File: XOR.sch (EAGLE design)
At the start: 60 parts, among them IC1 40106D, IC2 4030D, IC3 4520D, IC7 TL074D

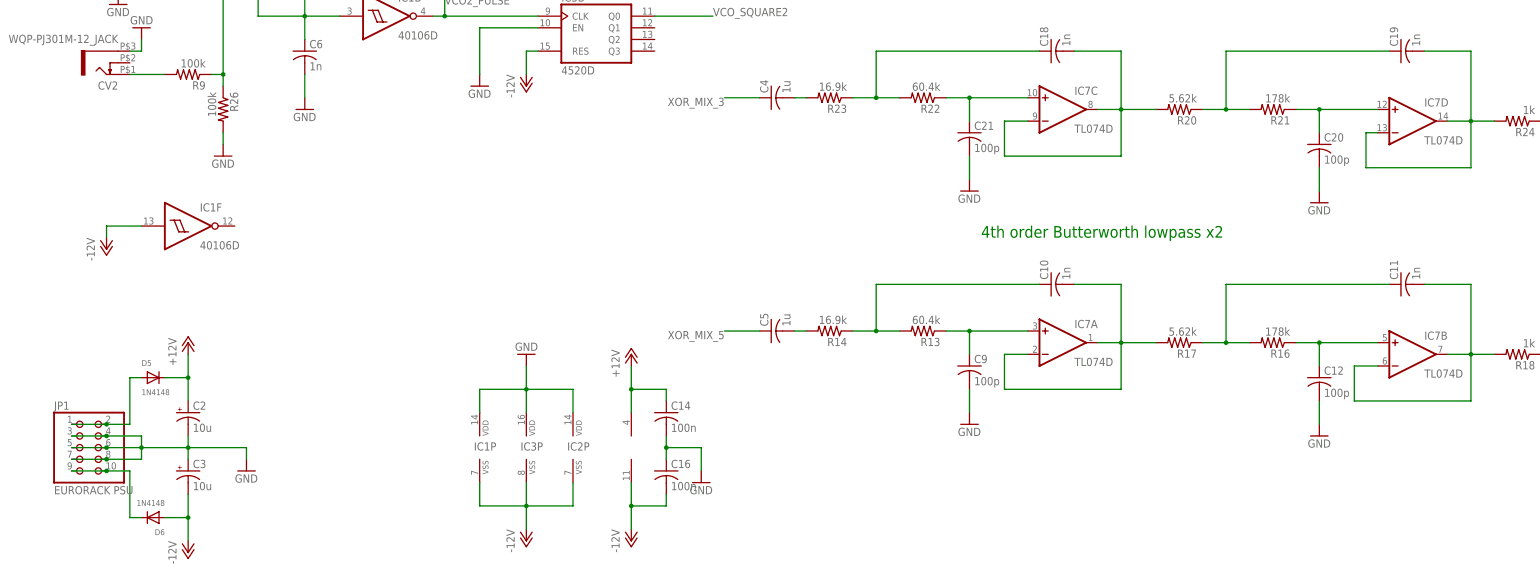
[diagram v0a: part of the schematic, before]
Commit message: added decoupling caps at logic ICs.
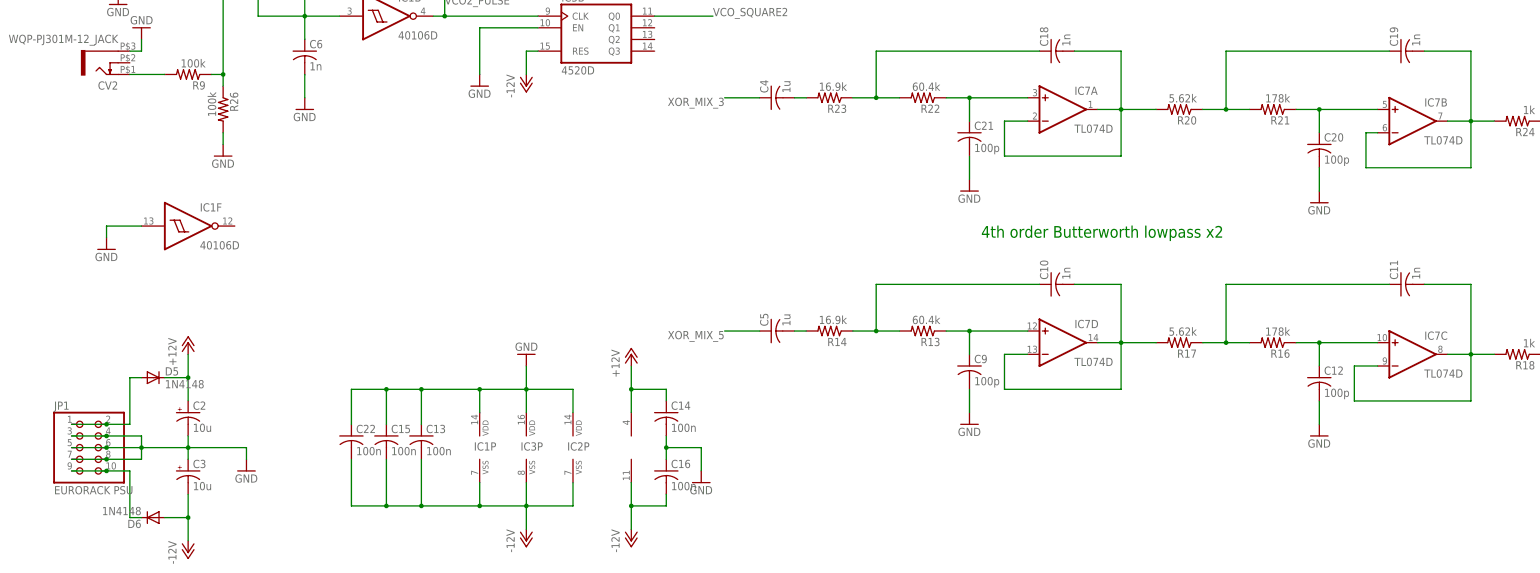
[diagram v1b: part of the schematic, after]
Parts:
- added C13, C15, C22: 100n, rcl:C-USC0603K
- D5, D6: device adafruit:DIODESOD-323F -> diode:DIODE-DO214AA
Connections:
- net -12V: now also C13.2, C15.2, C22.2; no longer IC1F.I
- net GND: now also C13.1, C15.1, C22.1, IC1F.I
- net N$16: now also IC7C.+IN; no longer IC7B.+IN
- net N$18: now also IC7D.-IN, IC7D.OUT; no longer IC7A.-IN, IC7A.OUT
- net N$22: now also IC7D.+IN; no longer IC7A.+IN
- net N$29: now also IC7A.-IN, IC7A.OUT; no longer IC7C.-IN, IC7C.OUT
- net N$30: now also IC7A.+IN; no longer IC7C.+IN
- net N$32: now also IC7C.-IN, IC7C.OUT; no longer IC7B.-IN, IC7B.OUT
- net N$35: now also IC7B.+IN; no longer IC7D.+IN
- net N$36: now also IC7B.-IN, IC7B.OUT; no longer IC7D.-IN, IC7D.OUT
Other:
- moved on the sheet: IC7A, IC7B, IC7C, IC7D
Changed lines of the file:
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@@
 <part name="GND13" library="supply1" deviceset="GND" device=""/>
 <part name="GND14" library="supply1" deviceset="GND" device=""/>
-<part name="D5" library="adafruit" deviceset="DIODE" device="SOD-323F" value="1N4148"/>
-<part name="D6" library="adafruit" deviceset="DIODE" device="SOD-323F" value="1N4148"/>
+<part name="D5" library="diode" deviceset="DIODE-" device="DO214AA" value="1N4148"/>
+<part name="D6" library="diode" deviceset="DIODE-" device="DO214AA" value="1N4148"/>
 <part name="D7" library="adafruit" deviceset="DIODE" device="SOD-323F" value="1N4148"/>
 <part name="D8" library="adafruit" deviceset="DIODE" device="SOD-323F" value="1N4148"/>
@@
 <part name="C4" library="rcl" deviceset="C-US" device="C0603K" value="1u"/>
 <part name="C5" library="rcl" deviceset="C-US" device="C0603K" value="1u"/>
-<part name="P-2" library="supply1" deviceset="-12V" device=""/>
 <part name="P-3" library="supply1" deviceset="-12V" device=""/>
 <part name="P-4" library="supply1" deviceset="-12V" device=""/>
@@
 <part name="P+1" library="supply1" deviceset="+12V" device=""/>
 <part name="P+2" library="supply1" deviceset="+12V" device=""/>
+<part name="GND23" library="supply1" deviceset="GND" device=""/>
+<part name="C13" library="rcl" deviceset="C-US" device="C0603K" value="100n"/>
+<part name="C15" library="rcl" deviceset="C-US" device="C0603K" value="100n"/>
+<part name="C22" library="rcl" deviceset="C-US" device="C0603K" value="100n"/>
 </parts>
 <sheets>
@@
 <instance part="C7" gate="G$1" x="208.28" y="193.04"/>
 <instance part="C17" gate="G$1" x="299.72" y="193.04"/>
-<instance part="IC7" gate="A" x="238.76" y="63.5"/>
-<instance part="IC7" gate="B" x="314.96" y="60.96"/>
-<instance part="IC7" gate="C" x="238.76" y="114.3"/>
-<instance part="IC7" gate="D" x="314.96" y="111.76"/>
+<instance part="IC7" gate="D" x="238.76" y="63.5"/>
+<instance part="IC7" gate="C" x="314.96" y="60.96"/>
+<instance part="IC7" gate="A" x="238.76" y="114.3"/>
+<instance part="IC7" gate="B" x="314.96" y="111.76"/>
 <instance part="IC7" gate="P" x="144.78" y="40.64"/>
 <instance part="C18" gate="G$1" x="236.22" y="127" rot="R90"/>
@@
 <instance part="C4" gate="G$1" x="175.26" y="116.84" rot="R90"/>
 <instance part="C5" gate="G$1" x="175.26" y="66.04" rot="R90"/>
-<instance part="P-2" gate="1" x="30.48" y="83.82"/>
 <instance part="P-3" gate="1" x="121.92" y="190.5"/>
 <instance part="P-4" gate="1" x="121.92" y="119.38"/>
@@
 <instance part="P+1" gate="1" x="33.02" y="233.68"/>
 <instance part="P+2" gate="1" x="33.02" y="162.56"/>
+<instance part="GND23" gate="1" x="30.48" y="83.82"/>
+<instance part="C13" gate="G$1" x="99.06" y="43.18"/>
+<instance part="C15" gate="G$1" x="91.44" y="43.18"/>
+<instance part="C22" gate="G$1" x="83.82" y="43.18"/>
 </instances>
 <busses>
@@
 <wire x1="121.92" y1="53.34" x2="121.92" y2="58.42" width="0.1524" layer="91"/>
 <pinref part="GND18" gate="1" pin="GND"/>
+<pinref part="C13" gate="G$1" pin="1"/>
+<wire x1="99.06" y1="45.72" x2="99.06" y2="53.34" width="0.1524" layer="91"/>
+<wire x1="99.06" y1="53.34" x2="111.76" y2="53.34" width="0.1524" layer="91"/>
+<pinref part="C15" gate="G$1" pin="1"/>
+<wire x1="91.44" y1="45.72" x2="91.44" y2="53.34" width="0.1524" layer="91"/>
+<wire x1="91.44" y1="53.34" x2="99.06" y2="53.34" width="0.1524" layer="91"/>
+<pinref part="C22" gate="G$1" pin="1"/>
+<wire x1="83.82" y1="45.72" x2="83.82" y2="53.34" width="0.1524" layer="91"/>
+<wire x1="83.82" y1="53.34" x2="91.44" y2="53.34" width="0.1524" layer="91"/>
+<junction x="91.44" y="53.34"/>
+<junction x="99.06" y="53.34"/>
+<junction x="111.76" y="53.34"/>
 </segment>
 <segment>
@@
 <wire x1="111.76" y1="132.08" x2="111.76" y2="121.92" width="0.1524" layer="91"/>
 <pinref part="GND22" gate="1" pin="GND"/>
+</segment>
+<segment>
+<pinref part="IC1" gate="F" pin="I"/>
+<wire x1="30.48" y1="88.9" x2="38.1" y2="88.9" width="0.1524" layer="91"/>
+<wire x1="30.48" y1="88.9" x2="30.48" y2="86.36" width="0.1524" layer="91"/>
+<pinref part="GND23" gate="1" pin="GND"/>
 </segment>
 </net>
@@
 <pinref part="R17" gate="G$1" pin="2"/>
 <wire x1="259.08" y1="63.5" x2="251.46" y2="63.5" width="0.1524" layer="91"/>
-<pinref part="IC7" gate="A" pin="-IN"/>
-<pinref part="IC7" gate="A" pin="OUT"/>
+<pinref part="IC7" gate="D" pin="-IN"/>
+<pinref part="IC7" gate="D" pin="OUT"/>
 </segment>
 </net>
@@
 <wire x1="218.44" y1="60.96" x2="218.44" y2="66.04" width="0.1524" layer="91"/>
 <junction x="218.44" y="66.04"/>
-<pinref part="IC7" gate="A" pin="+IN"/>
+<pinref part="IC7" gate="D" pin="+IN"/>
 </segment>
 </net>
@@
 <pinref part="R18" gate="G$1" pin="2"/>
 <junction x="327.66" y="60.96"/>
-<pinref part="IC7" gate="B" pin="-IN"/>
-<pinref part="IC7" gate="B" pin="OUT"/>
+<pinref part="IC7" gate="C" pin="-IN"/>
+<pinref part="IC7" gate="C" pin="OUT"/>
 </segment>
 </net>
@@
 <wire x1="294.64" y1="58.42" x2="294.64" y2="63.5" width="0.1524" layer="91"/>
 <junction x="294.64" y="63.5"/>
-<pinref part="IC7" gate="B" pin="+IN"/>
+<pinref part="IC7" gate="C" pin="+IN"/>
 </segment>
 </net>
@@
 <junction x="121.92" y="27.94"/>
 <pinref part="P-1" gate="1" pin="-12V"/>
-</segment>
-<segment>
-<pinref part="IC1" gate="F" pin="I"/>
-<wire x1="30.48" y1="88.9" x2="38.1" y2="88.9" width="0.1524" layer="91"/>
-<wire x1="30.48" y1="88.9" x2="30.48" y2="86.36" width="0.1524" layer="91"/>
-<pinref part="P-2" gate="1" pin="-12V"/>
+<pinref part="C13" gate="G$1" pin="2"/>
+<wire x1="99.06" y1="38.1" x2="99.06" y2="27.94" width="0.1524" layer="91"/>
+<wire x1="99.06" y1="27.94" x2="111.76" y2="27.94" width="0.1524" layer="91"/>
+<pinref part="C15" gate="G$1" pin="2"/>
+<wire x1="91.44" y1="38.1" x2="91.44" y2="27.94" width="0.1524" layer="91"/>
+<wire x1="91.44" y1="27.94" x2="99.06" y2="27.94" width="0.1524" layer="91"/>
+<pinref part="C22" gate="G$1" pin="2"/>
+<wire x1="83.82" y1="38.1" x2="83.82" y2="27.94" width="0.1524" layer="91"/>
+<wire x1="83.82" y1="27.94" x2="91.44" y2="27.94" width="0.1524" layer="91"/>
+<junction x="111.76" y="27.94"/>
+<junction x="99.06" y="27.94"/>
+<junction x="91.44" y="27.94"/>
 </segment>
 <segment>
@@
 <segment>
 <pinref part="R20" gate="G$1" pin="2"/>
-<pinref part="IC7" gate="C" pin="OUT"/>
+<pinref part="IC7" gate="A" pin="OUT"/>
 <wire x1="259.08" y1="114.3" x2="251.46" y2="114.3" width="0.1524" layer="91"/>
 <wire x1="251.46" y1="114.3" x2="246.38" y2="114.3" width="0.1524" layer="91"/>
@@
 <pinref part="C18" gate="G$1" pin="2"/>
 <wire x1="251.46" y1="127" x2="241.3" y2="127" width="0.1524" layer="91"/>
-<pinref part="IC7" gate="C" pin="-IN"/>
+<pinref part="IC7" gate="A" pin="-IN"/>
 <wire x1="231.14" y1="111.76" x2="226.06" y2="111.76" width="0.1524" layer="91"/>
 <wire x1="226.06" y1="111.76" x2="226.06" y2="104.14" width="0.1524" layer="91"/>
@@
 <segment>
 <pinref part="R22" gate="G$1" pin="1"/>
-<pinref part="IC7" gate="C" pin="+IN"/>
+<pinref part="IC7" gate="A" pin="+IN"/>
 <wire x1="213.36" y1="116.84" x2="218.44" y2="116.84" width="0.1524" layer="91"/>
 <pinref part="C21" gate="G$1" pin="1"/>
@@
 <segment>
 <pinref part="R21" gate="G$1" pin="1"/>
-<pinref part="IC7" gate="D" pin="+IN"/>
+<pinref part="IC7" gate="B" pin="+IN"/>
 <wire x1="289.56" y1="114.3" x2="294.64" y2="114.3" width="0.1524" layer="91"/>
 <pinref part="C20" gate="G$1" pin="1"/>
@@
 <net name="N$36" class="0">
 <segment>
-<pinref part="IC7" gate="D" pin="-IN"/>
+<pinref part="IC7" gate="B" pin="-IN"/>
 <wire x1="307.34" y1="109.22" x2="304.8" y2="109.22" width="0.1524" layer="91"/>
 <wire x1="304.8" y1="109.22" x2="304.8" y2="101.6" width="0.1524" layer="91"/>
 <wire x1="304.8" y1="101.6" x2="327.66" y2="101.6" width="0.1524" layer="91"/>
 <wire x1="327.66" y1="101.6" x2="327.66" y2="111.76" width="0.1524" layer="91"/>
-<pinref part="IC7" gate="D" pin="OUT"/>
+<pinref part="IC7" gate="B" pin="OUT"/>
 <wire x1="327.66" y1="111.76" x2="322.58" y2="111.76" width="0.1524" layer="91"/>
 <pinref part="R24" gate="G$1" pin="2"/>

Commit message: Changed PSU diode type/footprint. Not fits DO214 package types. PCB: moved ICs a bit, better fit for CV in jack 1.
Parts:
- D5, D6: value 1N4148 -> 1N4004
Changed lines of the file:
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@@
 <part name="GND13" library="supply1" deviceset="GND" device=""/>
 <part name="GND14" library="supply1" deviceset="GND" device=""/>
-<part name="D5" library="diode" deviceset="DIODE-" device="DO214AA" value="1N4148"/>
-<part name="D6" library="diode" deviceset="DIODE-" device="DO214AA" value="1N4148"/>
+<part name="D5" library="diode" deviceset="DIODE-" device="DO214AA" value="1N4004"/>
+<part name="D6" library="diode" deviceset="DIODE-" device="DO214AA" value="1N4004"/>
 <part name="D7" library="adafruit" deviceset="DIODE" device="SOD-323F" value="1N4148"/>
 <part name="D8" library="adafruit" deviceset="DIODE" device="SOD-323F" value="1N4148"/>

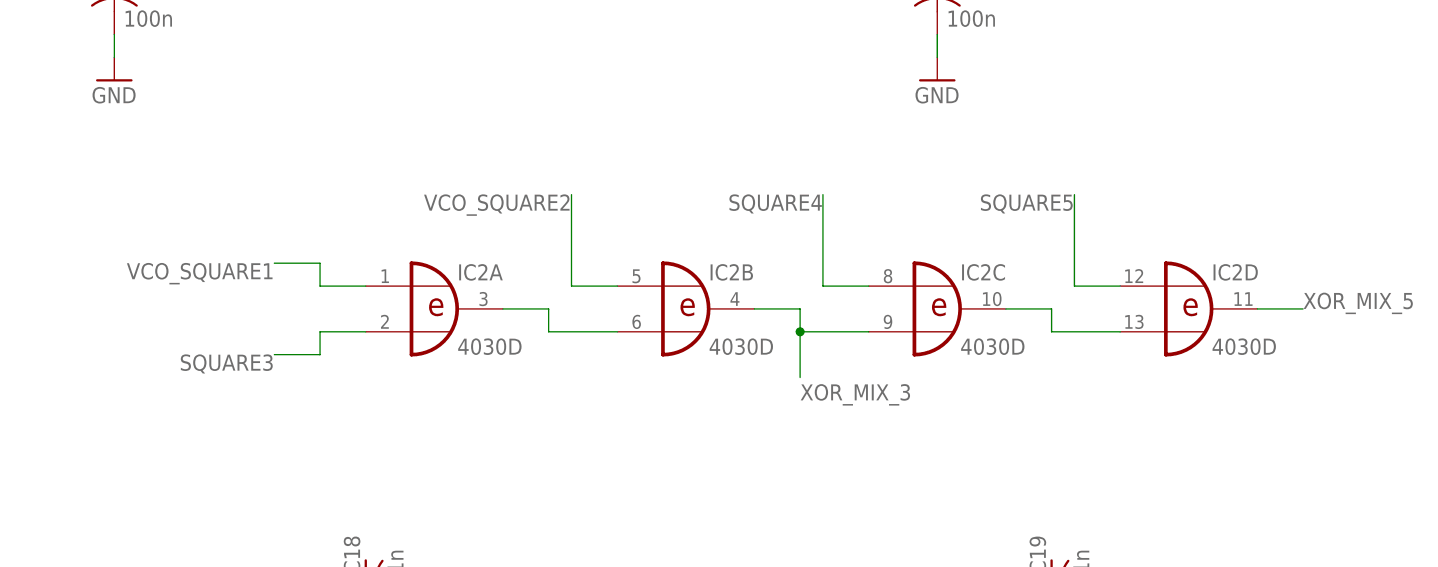
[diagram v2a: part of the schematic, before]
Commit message: Changed order in which oscillators are XORed together. Use bigger footprint for PSU smoothing caps. Moved XOR IC a bit & rerouted.
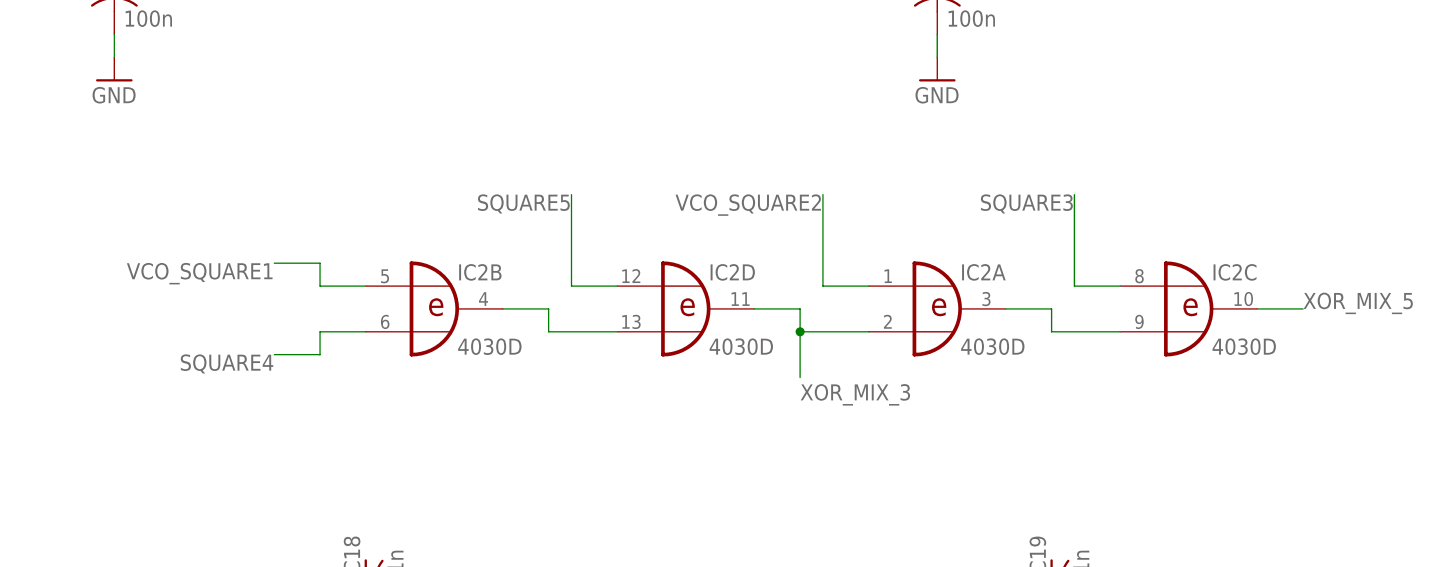
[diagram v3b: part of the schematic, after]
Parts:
- C2, C3: device rcl:CPOL-USC -> rcl:CPOL-USD
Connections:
- net N$10: now also IC2A.O, IC2C.I1; no longer IC2C.O, IC2D.I1
- net N$25: now also IC2B.O, IC2D.I1; no longer IC2A.O, IC2B.I1
- net SQUARE3: now also IC2C.I0; no longer IC2A.I1
- net SQUARE4: now also IC2B.I1; no longer IC2C.I0
- net VCO_SQUARE1: now also IC2B.I0; no longer IC2A.I0
- net VCO_SQUARE2: now also IC2A.I0; no longer IC2B.I0
- net XOR_MIX_3: now also IC2A.I1, IC2D.O; no longer IC2B.O, IC2C.I1
- net XOR_MIX_5: now also IC2C.O; no longer IC2D.O
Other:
- moved on the sheet: IC2A, IC2B, IC2C, IC2D
